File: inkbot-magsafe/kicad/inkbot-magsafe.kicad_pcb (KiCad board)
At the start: 4 copper layers, 60 x 99 mm, 0 parts

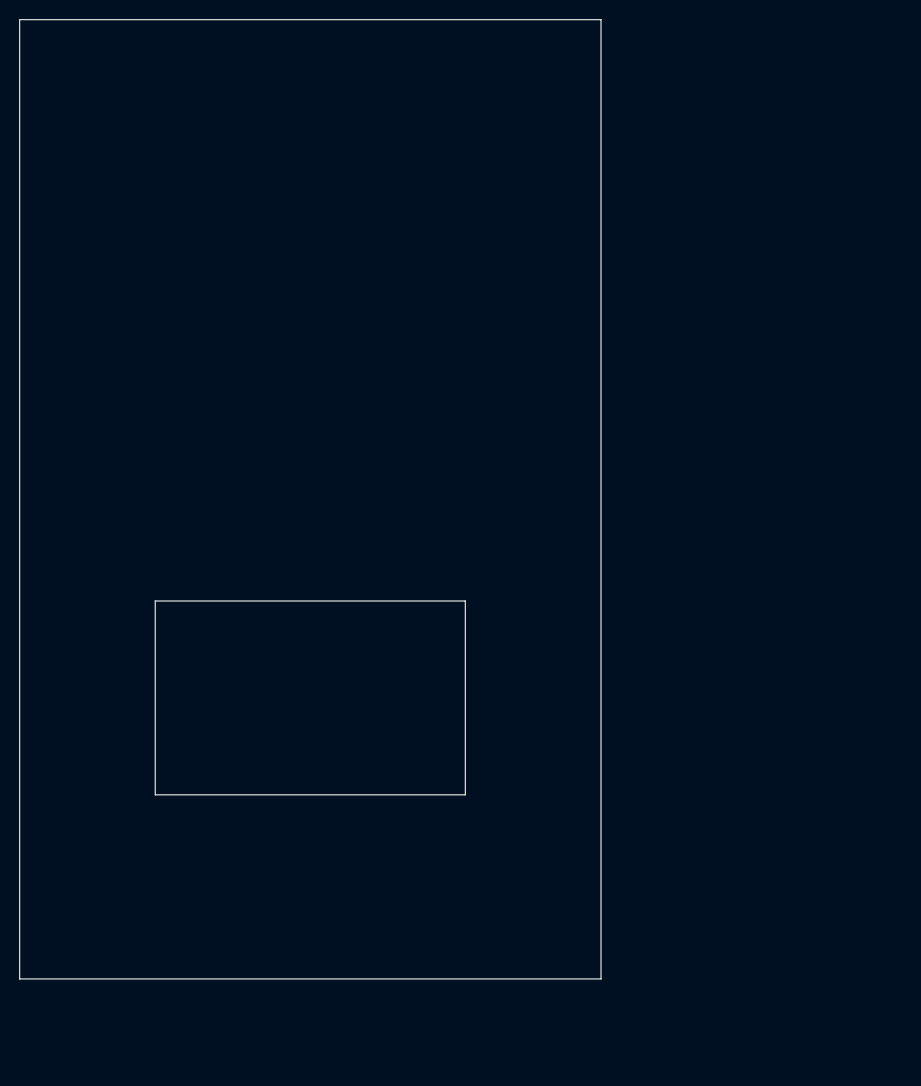
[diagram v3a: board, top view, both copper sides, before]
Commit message: inkbot-magsafe: route the board (planes + maze router) and export a fab set
Add kicad/layout_route.py: imports the schematic netlist, places the
module and support parts on the back around the coil and battery cutout,
assigns nets to every pad, pours In2/B.Cu ground and In1 VSYS planes,
maze-routes the signal nets (B.Cu with an F.Cu escape), fills the zones,
and exports Gerbers, drill, and centroid to kicad/fab/ (gitignored).

Antenna keep-out placed under the module's antenna end. First-pass result:
29/31 signal nets auto-routed with all four planes filled; a couple of nets
are left as ratsnest to finish in the KiCad GUI along with DRC. Replaces the
old place-only place_footprints.py.

Co-authored-by: Jason Hall <imjasonh@users.noreply.github.com>
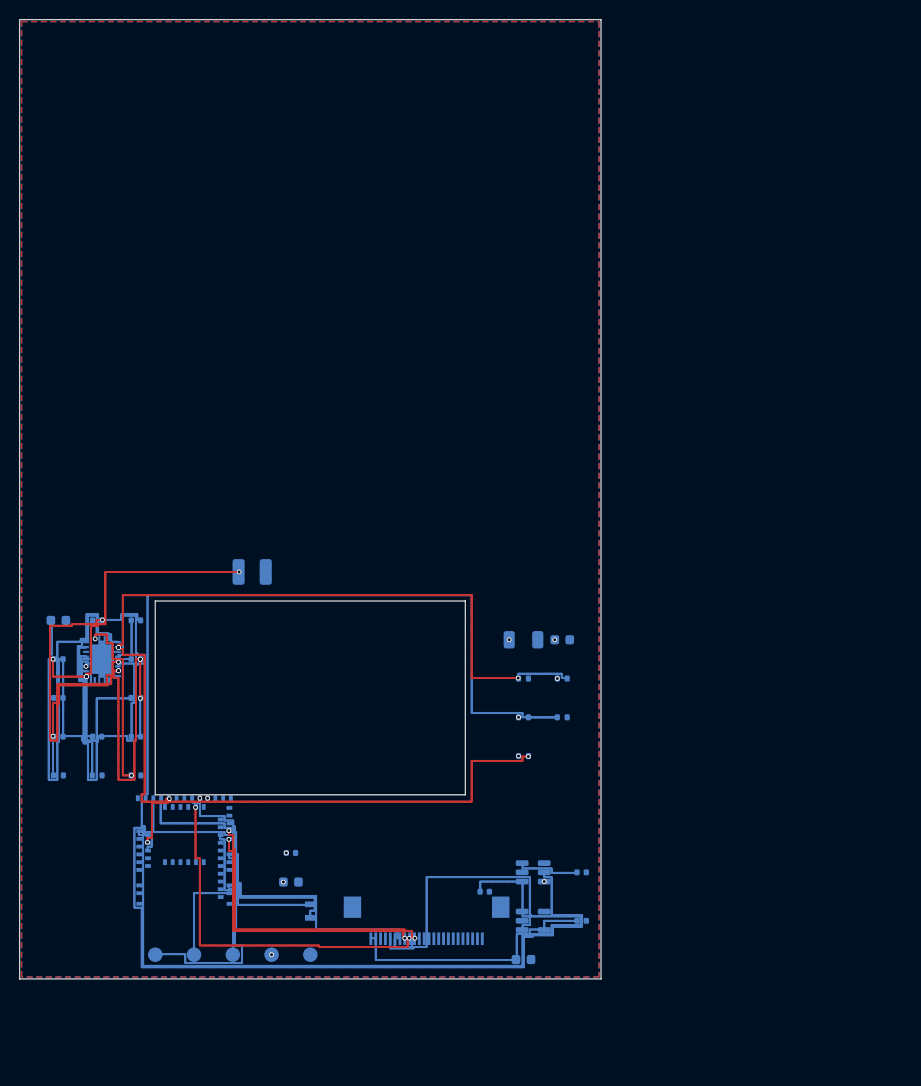
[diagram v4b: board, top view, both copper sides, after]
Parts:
- added C1: C_0603_1608Metric, C_0603_1608Metric, B.Cu at (4.00, 62.0)
- added C10: C_1206_3216Metric, C_1206_3216Metric, B.Cu at (52.0, 64.0)
- added C11: C_0603_1608Metric, C_0603_1608Metric, B.Cu at (56.0, 64.0)
- added C12: C_0402_1005Metric, C_0402_1005Metric, B.Cu at (58.0, 88.0)
- added C13: C_0402_1005Metric, C_0402_1005Metric, B.Cu at (48.0, 90.0)
- added C14: C_0402_1005Metric, C_0402_1005Metric, B.Cu at (58.0, 93.0)
- added C15: C_0402_1005Metric, C_0402_1005Metric, B.Cu at (28.0, 86.0)
- added C16: C_0603_1608Metric, C_0603_1608Metric, B.Cu at (28.0, 89.0)
- added C2: C_0402_1005Metric, C_0402_1005Metric, B.Cu at (4.00, 66.0)
- added C21: C_0603_1608Metric, C_0603_1608Metric, B.Cu at (52.0, 97.0)
- added C3: C_0402_1005Metric, C_0402_1005Metric, B.Cu at (4.00, 70.0)
- added C4: C_0402_1005Metric, C_0402_1005Metric, B.Cu at (8.00, 62.0)
- added C5: C_0402_1005Metric, C_0402_1005Metric, B.Cu at (12.0, 62.0)
- added C6: C_0402_1005Metric, C_0402_1005Metric, B.Cu at (12.0, 66.0)
- added C7: C_0402_1005Metric, C_0402_1005Metric, B.Cu at (4.00, 74.0)
- added C8: C_0402_1005Metric, C_0402_1005Metric, B.Cu at (8.00, 74.0)
- added C9: C_0402_1005Metric, C_0402_1005Metric, B.Cu at (12.0, 74.0)
- added J1: Hirose_FH12-24S-0.5SH_1x24-1MP_P0.50mm_Horizontal, Hirose_FH12-24S-0.5SH_1x24-1MP_P0.50mm_Horizontal, B.Cu at (42.0, 93.0)
- added L1: L_1210_3225Metric, L_1210_3225Metric, B.Cu at (24.0, 57.0)
- added R1: R_0402_1005Metric, R_0402_1005Metric, B.Cu at (4.00, 78.0)
- added R2: R_0402_1005Metric, R_0402_1005Metric, B.Cu at (8.00, 78.0)
- added R3: R_0402_1005Metric, R_0402_1005Metric, B.Cu at (12.0, 78.0)
- added R4: R_0402_1005Metric, R_0402_1005Metric, B.Cu at (12.0, 70.0)
- added R5: R_0402_1005Metric, R_0402_1005Metric, B.Cu at (56.0, 68.0)
- added R6: R_0402_1005Metric, R_0402_1005Metric, B.Cu at (52.0, 72.0)
- added R7: R_0402_1005Metric, R_0402_1005Metric, B.Cu at (56.0, 72.0)
- added R8: R_0402_1005Metric, R_0402_1005Metric, B.Cu at (52.0, 76.0)
- added RT1: R_0402_1005Metric, R_0402_1005Metric, B.Cu at (52.0, 68.0)
- added TP1: TestPoint_Pad_D1.5mm, TestPoint_Pad_D1.5mm, B.Cu at (14.0, 96.5)
- added TP2: TestPoint_Pad_D1.5mm, TestPoint_Pad_D1.5mm, B.Cu at (18.0, 96.5)
- added TP3: TestPoint_Pad_D1.5mm, TestPoint_Pad_D1.5mm, B.Cu at (22.0, 96.5)
- added TP4: TestPoint_Pad_D1.5mm, TestPoint_Pad_D1.5mm, B.Cu at (26.0, 96.5)
- added TP5: TestPoint_Pad_D1.5mm, TestPoint_Pad_D1.5mm, B.Cu at (30.0, 96.5)
- added U1: Raytac_MDBT50Q, Raytac_MDBT50Q, B.Cu at (17.0, 87.5)
- added U3: SOT-23-6, SOT-23-6, B.Cu at (53.0, 88.0)
- added U4: SOT-23-5, SOT-23-5, B.Cu at (53.0, 93.0)
- added U5: Texas_VQFN-RHL-20, Texas_VQFN-RHL-20, B.Cu at (8.50, 66.0)
- added Y1: Crystal_SMD_2012-2Pin_2.0x1.2mm, Crystal_SMD_2012-2Pin_2.0x1.2mm, B.Cu at (30.0, 92.0)
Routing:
- net /QI_RECT: track 0.00 -> 128.5 mm, vias 0 -> 6
- net /PANEL_BUSY: track 0.00 -> 96.7 mm
- net /VBAT_SENSE: track 0.00 -> 86.4 mm
- net /NTC_SENSE: track 0.00 -> 83.3 mm, vias 0 -> 4
- net /PANEL_PWR_EN: track 0.00 -> 76.4 mm
- net /CHG_STAT: track 0.00 -> 48.1 mm, vias 0 -> 2
- net /PANEL_RST: track 0.00 -> 40.7 mm
- net /PANEL_SCLK: track 0.00 -> 37.3 mm, vias 0 -> 2
- net /AC1: track 0.00 -> 31.8 mm, vias 0 -> 4
- net /PANEL_MOSI: track 0.00 -> 30.3 mm, vias 0 -> 2
- net /XL2: track 0.00 -> 28.7 mm
- net /PANEL_CS: track 0.00 -> 28.4 mm, vias 0 -> 2
- net /V3V3_PANEL: track 0.00 -> 27.4 mm
- net /XL1: track 0.00 -> 27.2 mm
- net /PANEL_DC: track 0.00 -> 26.4 mm
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- added copper zone on In1.Cu, net /VSYS
- added copper zone on B.Cu, net GND
- added copper zone on F.Cu, net GND
- added copper zone on In2.Cu, net GND

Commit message: inkbot-magsafe: clearance-correct router + real DRC/ERC (1067->49)
Run KiCad's actual DRC engine (pcbnew.WriteDRCReport) from run_drc.py
instead of a geometry approximation; kicad-cli pcb drc is KiCad 8+ only
and the PPA/Flathub/Snap/downloads are outside the sandbox egress.

Rework layout_route.py so the auto-route is clearance-correct: 0.2 mm
grid with a neighbour clearance check, honor the Raytac module's antenna
keep-outs, board-edge/cutout and via-halo margins, and via/stub fanout
to the planes. Move the module below the cutout (rotated) and the LFXO
out of its keep-out. This cuts DRC from 1067 to 49 error-severity
violations; the rest are 0.5 mm-pitch fanout and the dense bottom
cluster, left to finish in the GUI.

Add run_erc.py (netlist electrical rules + board parity) since KiCad 7
has no sch erc: ERC is clean, 13/13 critical nets, parity holds.

Co-authored-by: Jason Hall <imjasonh@users.noreply.github.com>
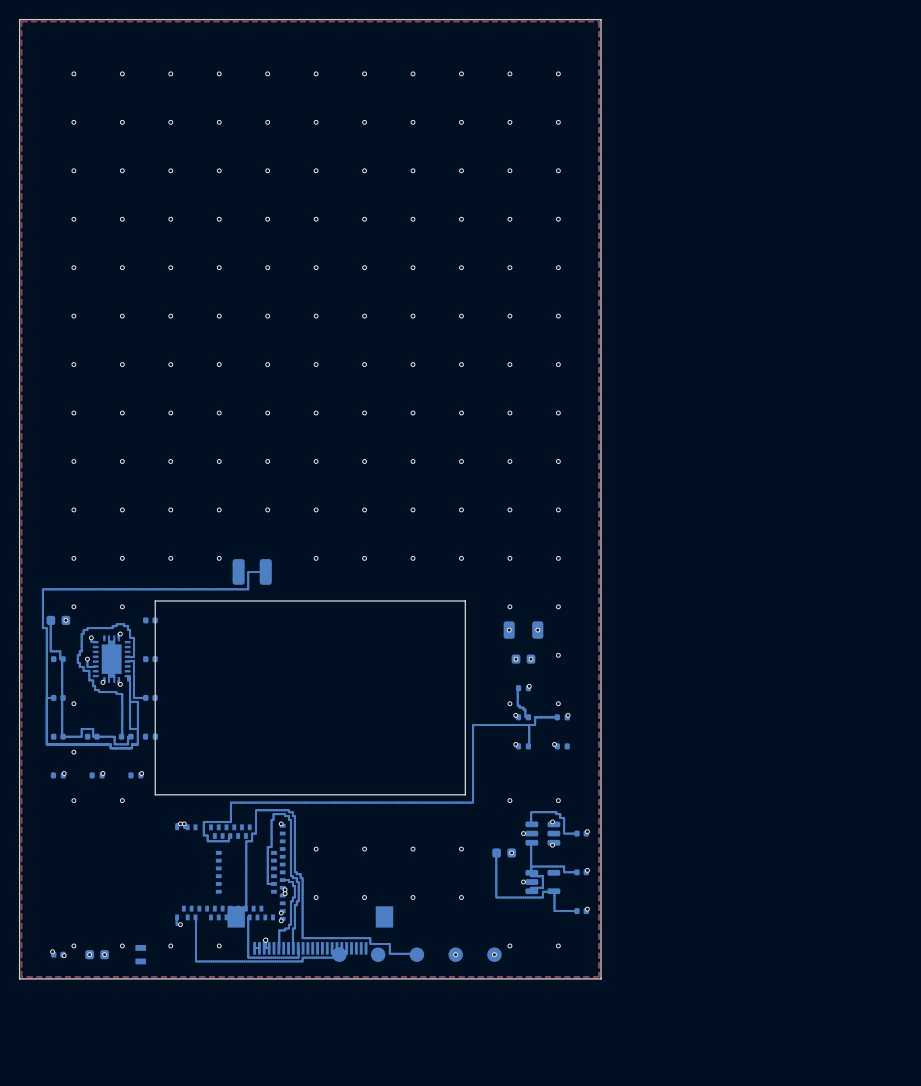
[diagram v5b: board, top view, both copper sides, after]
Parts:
- moved C15 26.2 mm to (4.00, 96.5)
- moved C16 21.4 mm to (8.00, 96.5)
- moved TP1 19.0 mm to (33.0, 96.5)
- moved TP2 19.0 mm to (37.0, 96.5)
- moved TP3 19.0 mm to (41.0, 96.5)
- moved TP4 19.0 mm to (45.0, 96.5)
- moved TP5 19.0 mm to (49.0, 96.5)
- moved Y1 18.1 mm to (12.5, 96.5)
- moved C4 12.6 mm to (4.00, 74.0)
- moved J1 12.0 mm to (30.0, 94.0)
- moved C21 11.2 mm to (50.0, 86.0)
- moved C7 10.3 mm to (13.5, 70.0)
- moved C13 10.2 mm to (58.0, 88.0)
- moved R5 5.66 mm to (52.0, 72.0)
- moved C11 4.47 mm to (52.0, 66.0)
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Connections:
- U1 pad 12: (no net) -> /PANEL_PWR_EN
- U1 pad 13: /PANEL_PWR_EN -> (no net)
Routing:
- net /QI_RECT: track 128.5 -> 23.4 mm, vias 6 -> 0
- net /PANEL_BUSY: track 96.7 -> 0.00 mm
- net /AC2: track 0.00 -> 83.2 mm
- net /NTC_SENSE: track 83.3 -> 4.20 mm, vias 4 -> 0
- net /PANEL_PWR_EN: track 76.4 -> 0.00 mm
- net /CHG_STAT: track 48.1 -> 0.00 mm, vias 2 -> 0
- net /AC1: track 31.8 -> 0.00 mm, vias 4 -> 0
- net /PANEL_RST: track 40.7 -> 9.80 mm
- net /NRST: track 13.7 -> 42.6 mm
- net /XL2: track 28.7 -> 0.00 mm
- net /PANEL_CS: track 28.4 -> 0.00 mm, vias 2 -> 0
- net /VBAT_SENSE: track 86.4 -> 58.4 mm
- net /XL1: track 27.2 -> 0.00 mm
- net /PANEL_DC: track 26.4 -> 0.00 mm
- net /QI_ILIM: track 26.3 -> 0.00 mm
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
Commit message: inkbot-magsafe: route the board to clean DRC
Co-authored-by: Jason Hall <imjasonh@users.noreply.github.com>
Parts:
- moved R3 16.9 mm to (8.45, 61.5), turned to -90 degrees
- moved R2 16.6 mm to (12.5, 62.0)
- moved J1 14.0 mm to (44.0, 94.0)
- moved TP1 13.6 mm to (31.5, 83.0)
- moved TP4 13.6 mm to (31.5, 95.0)
- moved TP2 11.0 mm to (31.5, 87.0)
- moved TP3 11.0 mm to (31.5, 91.0)
- moved C9 9.62 mm to (12.5, 64.5)
- moved TP5 7.57 mm to (56.5, 95.5)
- moved C14 7.11 mm to (52.5, 87.5)
- moved U4 6.96 mm to (56.5, 82.5)
- moved C13 6.26 mm to (52.5, 85.0)
- moved C6 6.08 mm to (12.5, 72.0)
- moved C12 5.85 mm to (52.5, 82.0)
- moved U3 5.70 mm to (48.5, 82.5)
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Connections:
- U1 pad 12: /PANEL_PWR_EN -> (no net)
- U1 pad 13: (no net) -> /PANEL_PWR_EN
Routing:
- net /VSYS: track 4.40 -> 126.8 mm, vias 12 -> 5
- net /CHG_STAT: track 0.00 -> 74.4 mm, vias 0 -> 3
- net /NTC_SENSE: track 4.20 -> 78.3 mm, vias 0 -> 4
- net /AC2: track 83.2 -> 33.2 mm, vias 0 -> 3
- net /AC1: track 0.00 -> 30.4 mm, vias 0 -> 3
- net /NRST: track 42.6 -> 12.6 mm, vias 0 -> 2
- net /PANEL_PWR_EN: track 0.00 -> 29.0 mm, vias 0 -> 2
- net /QI_RECT: track 23.4 -> 49.5 mm
- net /PANEL_BUSY: track 0.00 -> 24.9 mm, vias 0 -> 2
- net /QI_COMM2: track 26.0 -> 2.40 mm
- net /PANEL_DC: track 0.00 -> 23.5 mm, vias 0 -> 2
- net /QI_ILIM: track 0.00 -> 22.6 mm, vias 0 -> 2
- net /PANEL_CS: track 0.00 -> 21.7 mm, vias 0 -> 2
- net /XL2: track 0.00 -> 20.0 mm, vias 0 -> 2
- net /XL1: track 0.00 -> 19.8 mm, vias 0 -> 2
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- removed copper zone on In1.Cu, net /VSYS

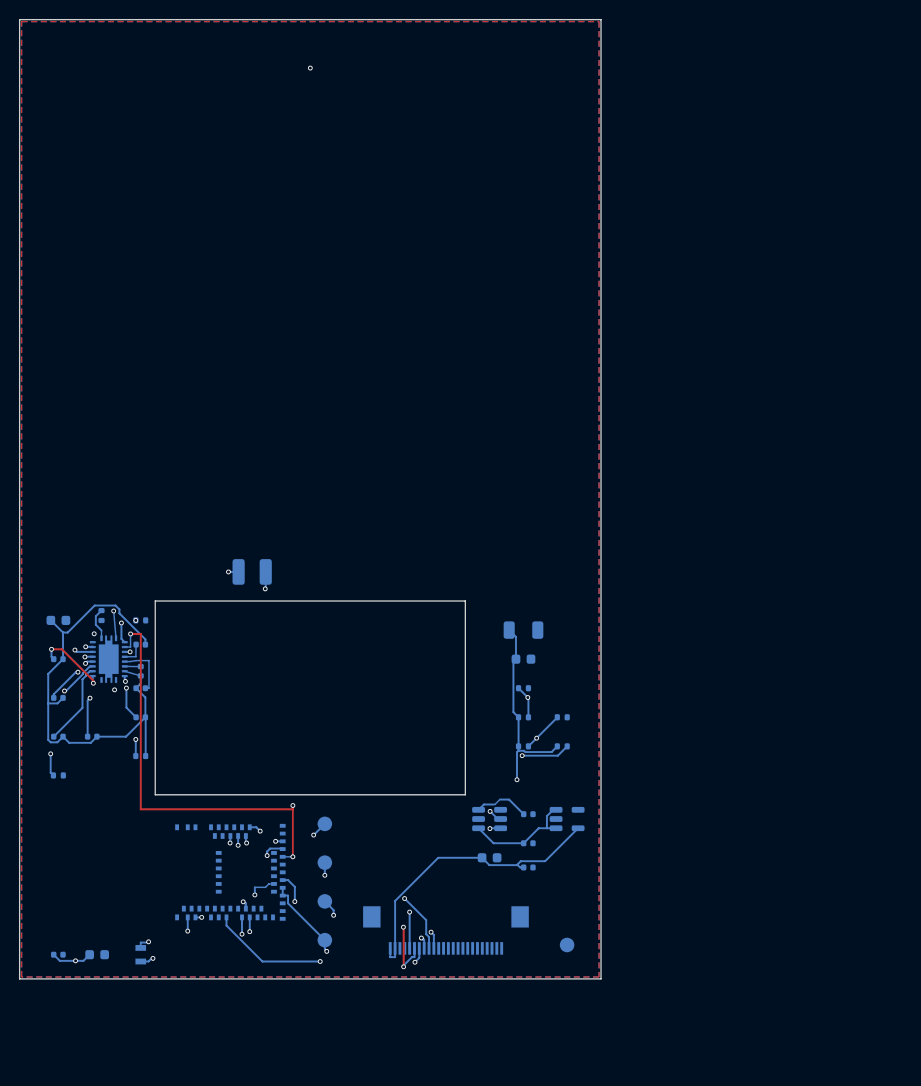
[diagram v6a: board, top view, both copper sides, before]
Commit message: inkbot-magsafe: regenerate the EVT board outline
Co-authored-by: Jason Hall <imjasonh@users.noreply.github.com>
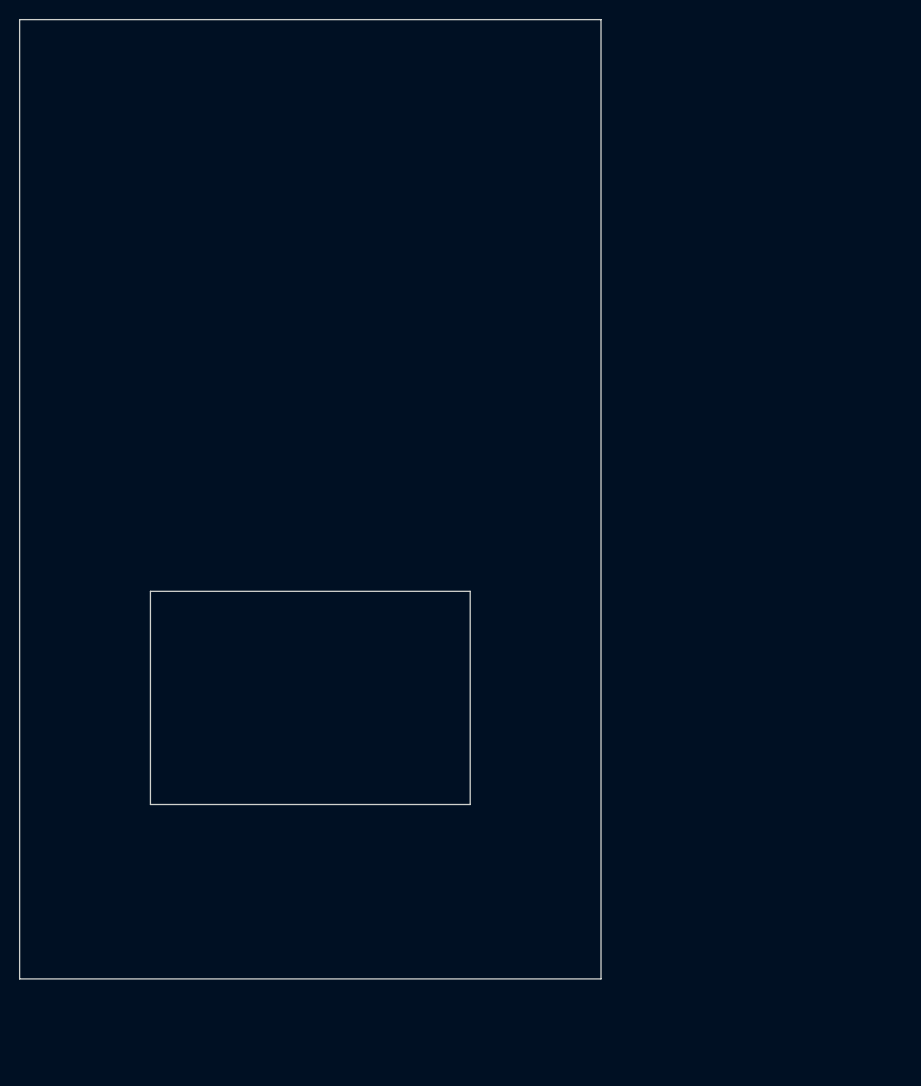
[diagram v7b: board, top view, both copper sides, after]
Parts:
- removed C1, C11, C16, C21: C_0603_1608Metric, C_0603_1608Metric
- removed C10: C_1206_3216Metric, C_1206_3216Metric
- removed C12, C13, C14, C15, C2, C3, C4, C5, C6, C7, C8, C9: C_0402_1005Metric, C_0402_1005Metric
- removed J1: Hirose_FH12-24S-0.5SH_1x24-1MP_P0.50mm_Horizontal, Hirose_FH12-24S-0.5SH_1x24-1MP_P0.50mm_Horizontal
- removed L1: L_1210_3225Metric, L_1210_3225Metric
- removed R1, R2, R3, R4, R5, R6, R7, R8, RT1: R_0402_1005Metric, R_0402_1005Metric
- removed TP1, TP2, TP3, TP4, TP5: TestPoint_Pad_D1.5mm, TestPoint_Pad_D1.5mm
- removed U1: Raytac_MDBT50Q, Raytac_MDBT50Q
- removed U3: SOT-23-6, SOT-23-6
- removed U4: SOT-23-5, SOT-23-5
- removed U5: Texas_VQFN-RHL-20, Texas_VQFN-RHL-20
- removed Y1: Crystal_SMD_2012-2Pin_2.0x1.2mm, Crystal_SMD_2012-2Pin_2.0x1.2mm
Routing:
- net /VSYS: track 126.8 -> 0.00 mm, vias 5 -> 0
- net /NTC_SENSE: track 78.3 -> 0.00 mm, vias 4 -> 0
- net /CHG_STAT: track 74.4 -> 0.00 mm, vias 3 -> 0
- net /QI_RECT: track 49.5 -> 0.00 mm
- net /VBAT_SENSE: track 41.7 -> 0.00 mm, vias 2 -> 0
- net /AC2: track 33.2 -> 0.00 mm, vias 3 -> 0
- net /V3V3_PANEL: track 30.6 -> 0.00 mm
- net /AC1: track 30.4 -> 0.00 mm, vias 3 -> 0
- net /PANEL_PWR_EN: track 29.0 -> 0.00 mm, vias 2 -> 0
- net /PANEL_BUSY: track 24.9 -> 0.00 mm, vias 2 -> 0
- net /PANEL_SCLK: track 24.7 -> 0.00 mm, vias 2 -> 0
- net /PANEL_DC: track 23.5 -> 0.00 mm, vias 2 -> 0
- net /QI_ILIM: track 22.6 -> 0.00 mm, vias 2 -> 0
- net /PANEL_MOSI: track 22.0 -> 0.00 mm, vias 2 -> 0
- net /PANEL_RST: track 22.0 -> 0.00 mm, vias 3 -> 0
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- removed copper zone on B.Cu, net GND
- removed copper zone on F.Cu, net GND
- removed copper zone on In2.Cu, net GND
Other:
- outline, holes or cut-outs redrawn
- board text added: "54 x 46 mm EVT magnetic array"
- board text added: "EVT geometry; production magnet data requires MFi approval"
- board text added: "GDEM0397T81P panel outline"
- board text added: "LP252030 protected-cell cutout"
- board text added: "WR222230 coil shield"
- board text removed: "LiPo cutout"
- board text removed: "MagSafe ring PCD"
- board text removed: "Qi coil"
- board text removed: "panel 3.97in 480x800 (front, overlaps ring)"
- board text removed: "top edge <=30mm above ring center: clears camera bump"
